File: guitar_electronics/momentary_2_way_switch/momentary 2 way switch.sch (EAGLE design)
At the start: 8 parts

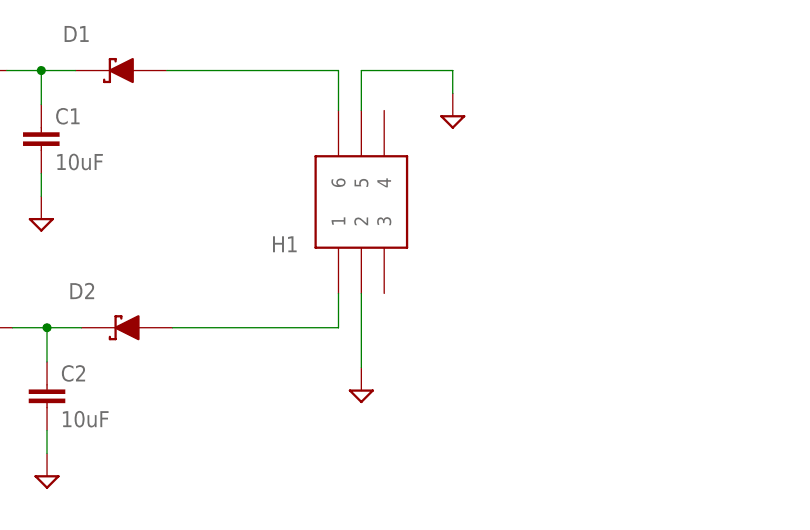
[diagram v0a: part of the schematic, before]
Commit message: updates for 2 way switch
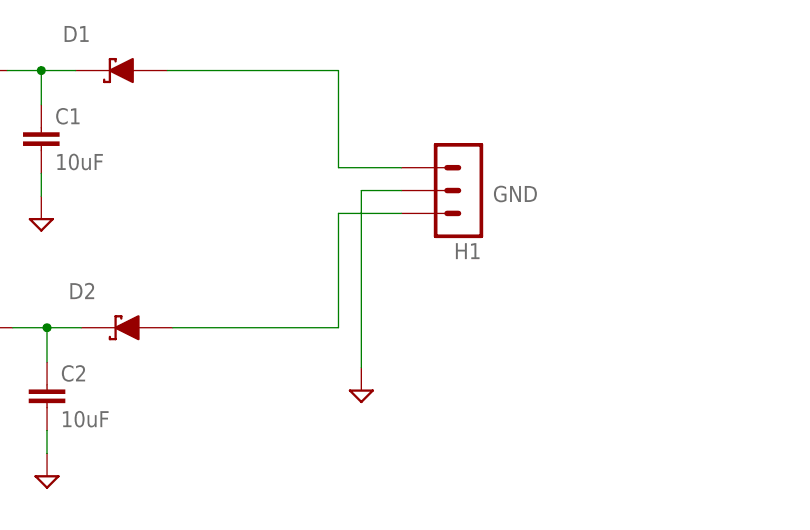
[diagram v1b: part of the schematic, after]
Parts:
- H1: value 6PIN-SMD-2.54MM_2 -> 3PIN-SMD-2.54MM; device CYCFI_Con:6PIN-SMD-2.54MM_2 -> CYCFI_Con:3PIN-SMD-2.54MM
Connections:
- net GND: no longer H1.5
- net SW1: now also H1.3; no longer H1.1
- net SW2: now also H1.1; no longer H1.6
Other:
- note added: "GND"
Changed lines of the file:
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@@
 <setting verticaltext="up"/>
 </settings>
-<grid distance="0.1" unitdist="inch" unit="inch" style="lines" multiple="1" display="no" altdistance="0.01" altunitdist="inch" altunit="inch"/>
+<grid distance="0.025" unitdist="inch" unit="inch" style="lines" multiple="1" display="yes" altdistance="0.01" altunitdist="inch" altunit="inch"/>
 <layers>
 <layer number="1" name="Top" color="4" fill="1" visible="no" active="no"/>
@@
 <part name="C2" library="resistor" deviceset="C-EU" device="C0603" value="10uF"/>
 <part name="S1" library="switch" deviceset="SPDT" device=""/>
-<part name="H1" library="CYCFI_Con" deviceset="6PIN-SMD-2.54MM_2" device=""/>
 <part name="SUPPLY3" library="supply2" deviceset="GND" device=""/>
-<part name="SUPPLY5" library="supply2" deviceset="GND" device=""/>
+<part name="H1" library="CYCFI_Con" deviceset="3PIN-SMD-2.54MM" device=""/>
 </parts>
 <sheets>
@@
 <rectangle x1="199.54875" y1="31.90875" x2="207.67675" y2="31.97225" layer="95"/>
 <rectangle x1="208.24825" y1="31.90875" x2="210.59775" y2="31.97225" layer="95"/>
+<text x="180.34" y="113.03" size="1.778" layer="95">GND</text>
 </plain>
 <instances>
@@
 <attribute name="VALUE" x="90.17" y="106.68" size="1.778" layer="96"/>
 </instance>
-<instance part="H1" gate="G$1" x="165.735" y="113.03" smashed="yes" rot="R90">
-<attribute name="NAME" x="158.75" y="109.22" size="1.778" layer="95" rot="R180"/>
+<instance part="SUPPLY3" gate="GND" x="165.735" y="92.075" smashed="yes"/>
+<instance part="H1" gate="G$1" x="177.8" y="114.3" smashed="yes" rot="R180">
+<attribute name="NAME" x="179.07" y="108.458" size="1.778" layer="95" rot="R180"/>
 </instance>
-<instance part="SUPPLY3" gate="GND" x="165.735" y="92.075" smashed="yes"/>
-<instance part="SUPPLY5" gate="GND" x="175.895" y="122.555" smashed="yes"/>
 </instances>
 <busses>
@@
 </segment>
 <segment>
-<pinref part="SUPPLY5" gate="GND" pin="GND"/>
-<wire x1="175.895" y1="125.095" x2="175.895" y2="127.635" width="0.1524" layer="91"/>
-<wire x1="175.895" y1="127.635" x2="165.735" y2="127.635" width="0.1524" layer="91"/>
-<pinref part="H1" gate="G$1" pin="5"/>
-<wire x1="165.735" y1="123.19" x2="165.735" y2="127.635" width="0.1524" layer="91"/>
-</segment>
-<segment>
 <pinref part="SUPPLY3" gate="GND" pin="GND"/>
 <pinref part="H1" gate="G$1" pin="2"/>
-<wire x1="165.735" y1="94.615" x2="165.735" y2="102.87" width="0.1524" layer="91"/>
+<wire x1="170.18" y1="114.3" x2="165.735" y2="114.3" width="0.1524" layer="91"/>
+<wire x1="165.735" y1="114.3" x2="165.735" y2="94.615" width="0.1524" layer="91"/>
 </segment>
 </net>
@@
 <pinref part="D1" gate="G$1" pin="A"/>
 <wire x1="163.195" y1="127.635" x2="144.145" y2="127.635" width="0.1524" layer="91"/>
-<pinref part="H1" gate="G$1" pin="6"/>
-<wire x1="163.195" y1="123.19" x2="163.195" y2="127.635" width="0.1524" layer="91"/>
+<pinref part="H1" gate="G$1" pin="1"/>
+<wire x1="170.18" y1="116.84" x2="163.195" y2="116.84" width="0.1524" layer="91"/>
+<wire x1="163.195" y1="116.84" x2="163.195" y2="127.635" width="0.1524" layer="91"/>
 </segment>
 </net>
@@
 <pinref part="D2" gate="G$1" pin="A"/>
 <wire x1="144.78" y1="99.06" x2="163.195" y2="99.06" width="0.1524" layer="91"/>
-<pinref part="H1" gate="G$1" pin="1"/>
-<wire x1="163.195" y1="99.06" x2="163.195" y2="102.87" width="0.1524" layer="91"/>
+<pinref part="H1" gate="G$1" pin="3"/>
+<wire x1="170.18" y1="111.76" x2="163.195" y2="111.76" width="0.1524" layer="91"/>
+<wire x1="163.195" y1="111.76" x2="163.195" y2="99.06" width="0.1524" layer="91"/>
 </segment>
 </net>

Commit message: add schematic and bom file
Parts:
- D1, D2: value (none) -> CUS551V30,H3F
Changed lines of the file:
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@@
 <setting verticaltext="up"/>
 </settings>
-<grid distance="0.025" unitdist="inch" unit="inch" style="lines" multiple="1" display="yes" altdistance="0.01" altunitdist="inch" altunit="inch"/>
+<grid distance="0.1" unitdist="inch" unit="inch" style="lines" multiple="1" display="no" altdistance="0.01" altunitdist="inch" altunit="inch"/>
 <layers>
 <layer number="1" name="Top" color="4" fill="1" visible="no" active="no"/>
@@
 <part name="R1" library="resistor" deviceset="R-EU_" device="R0402" value="1K"/>
 <part name="SUPPLY1" library="supply2" deviceset="GND" device=""/>
-<part name="D1" library="m-pad-2.1" deviceset="D_SCHOTTKY" device="L"/>
+<part name="D1" library="m-pad-2.1" deviceset="D_SCHOTTKY" device="L" value="CUS551V30,H3F"/>
 <part name="C1" library="resistor" deviceset="C-EU" device="C0603" value="10uF"/>
 <part name="SUPPLY2" library="supply2" deviceset="GND" device=""/>
 <part name="R2" library="resistor" deviceset="R-EU_" device="R0402" value="1K"/>
 <part name="SUPPLY4" library="supply2" deviceset="GND" device=""/>
-<part name="D2" library="m-pad-2.1" deviceset="D_SCHOTTKY" device="L"/>
+<part name="D2" library="m-pad-2.1" deviceset="D_SCHOTTKY" device="L" value="CUS551V30,H3F"/>
 <part name="C2" library="resistor" deviceset="C-EU" device="C0603" value="10uF"/>
 <part name="S1" library="switch" deviceset="SPDT" device=""/>
@@
 <instance part="D1" gate="G$1" x="139.065" y="127.635" smashed="yes" rot="R180">
 <attribute name="NAME" x="135.636" y="132.588" size="1.778" layer="95" rot="R180"/>
-<attribute name="VALUE" x="141.351" y="132.08" size="1.778" layer="96" rot="R180"/>
+<attribute name="VALUE" x="159.131" y="132.08" size="1.778" layer="96" rot="R180"/>
 </instance>
 <instance part="C1" gate="G$1" x="130.175" y="121.285"/>
@@
 <instance part="D2" gate="G$1" x="139.7" y="99.06" smashed="yes" rot="R180">
 <attribute name="NAME" x="136.271" y="104.013" size="1.778" layer="95" rot="R180"/>
-<attribute name="VALUE" x="141.986" y="103.505" size="1.778" layer="96" rot="R180"/>
+<attribute name="VALUE" x="159.766" y="103.505" size="1.778" layer="96" rot="R180"/>
 </instance>
 <instance part="C2" gate="G$1" x="130.81" y="92.71"/>
